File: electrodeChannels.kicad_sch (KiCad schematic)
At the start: 20 parts, among them Q17 PNP, Q2 NPN, Q20 PNP, Q5 PNP, Q8 PNP

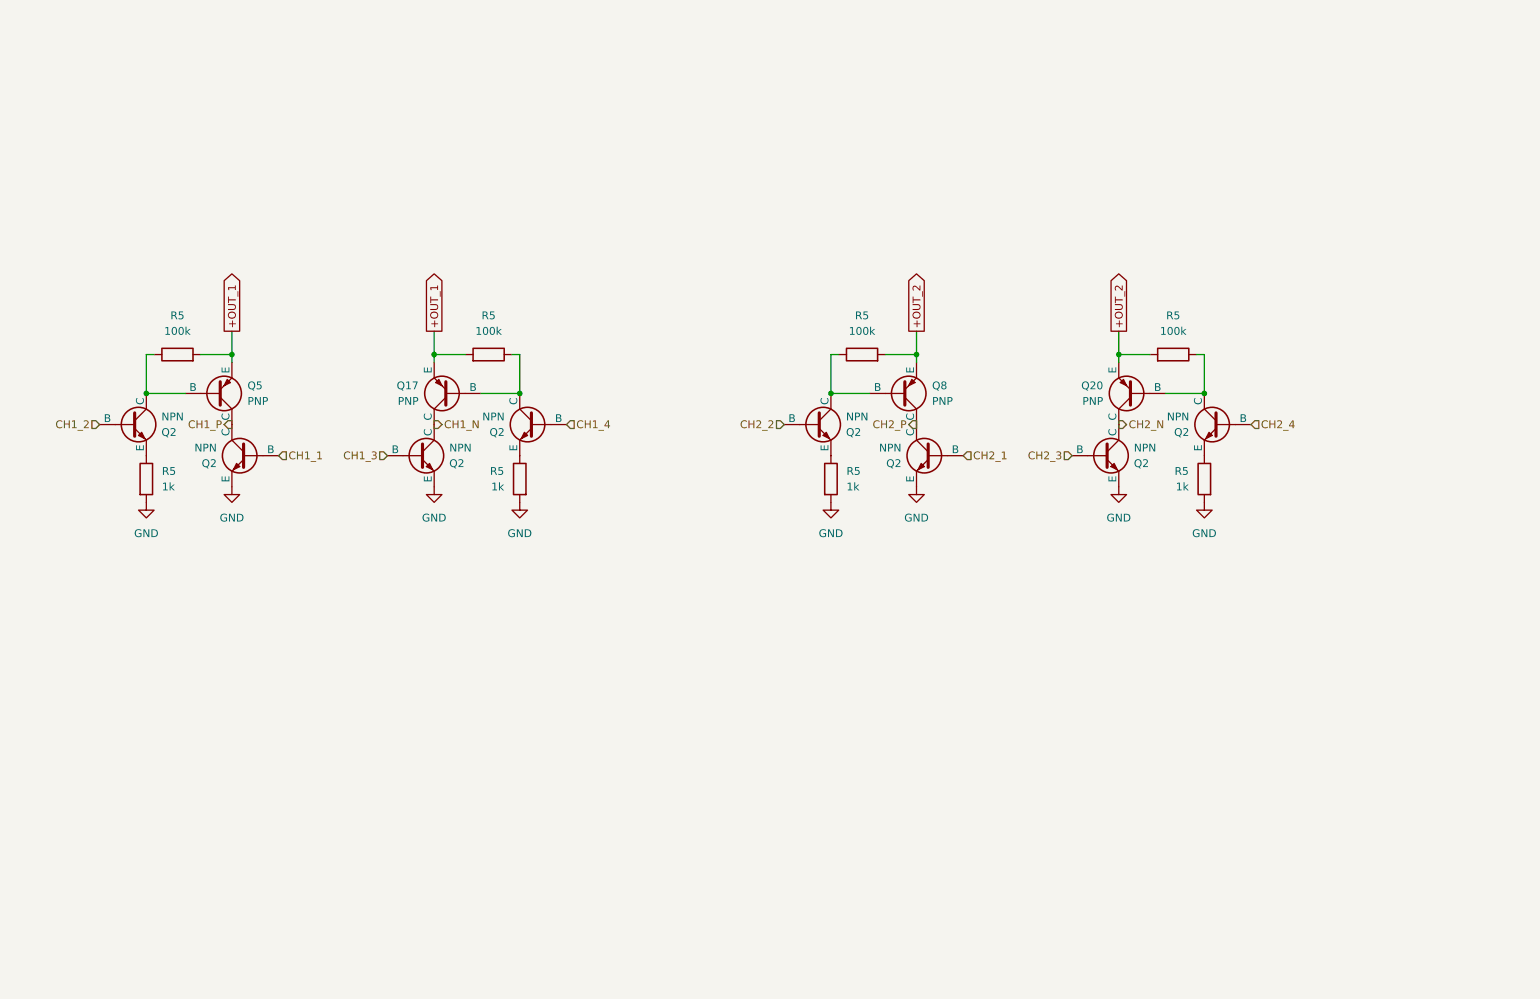
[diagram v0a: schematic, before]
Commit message: v3: removed digital potentiometer, added 8 discrete resistors and one GPIO expander
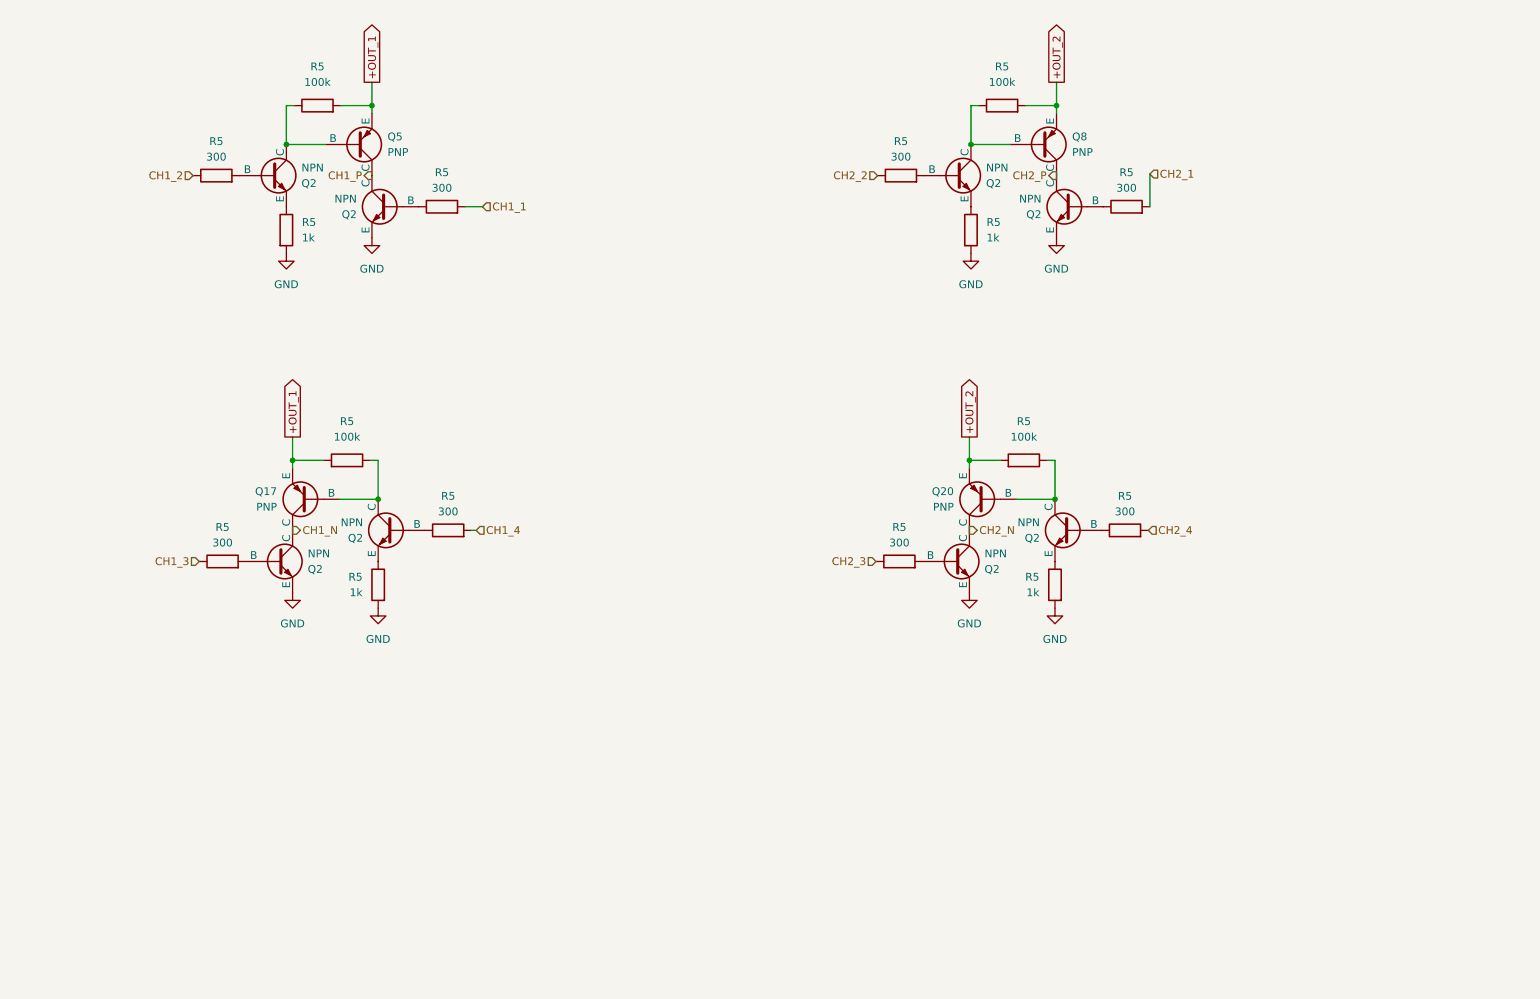
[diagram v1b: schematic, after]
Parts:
- added R5 (x8): 300, Resistor_SMD:R_0402_1005Metric, symbol Device:R
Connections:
- net CH1_1: now also R5.2; no longer Q2.1 (B)
- net CH1_2: now also R5.1; no longer Q2.1 (B)
- net CH1_3: now also R5.1; no longer Q2.1 (B)
- net CH1_4: now also R5.2; no longer Q2.1 (B)
- net CH2_1: now also R5.2; no longer Q2.1 (B)
- net CH2_2: now also R5.1; no longer Q2.1 (B)
- net CH2_3: now also R5.1; no longer Q2.1 (B)
- net CH2_4: now also R5.2; no longer Q2.1 (B)
- new net: Q2.1 (B), R5.1 (x4)
- new net: Q2.1 (B), R5.2 (x4)
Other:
- moved on the sheet: Q17, Q2, Q20, Q5, Q8, R5

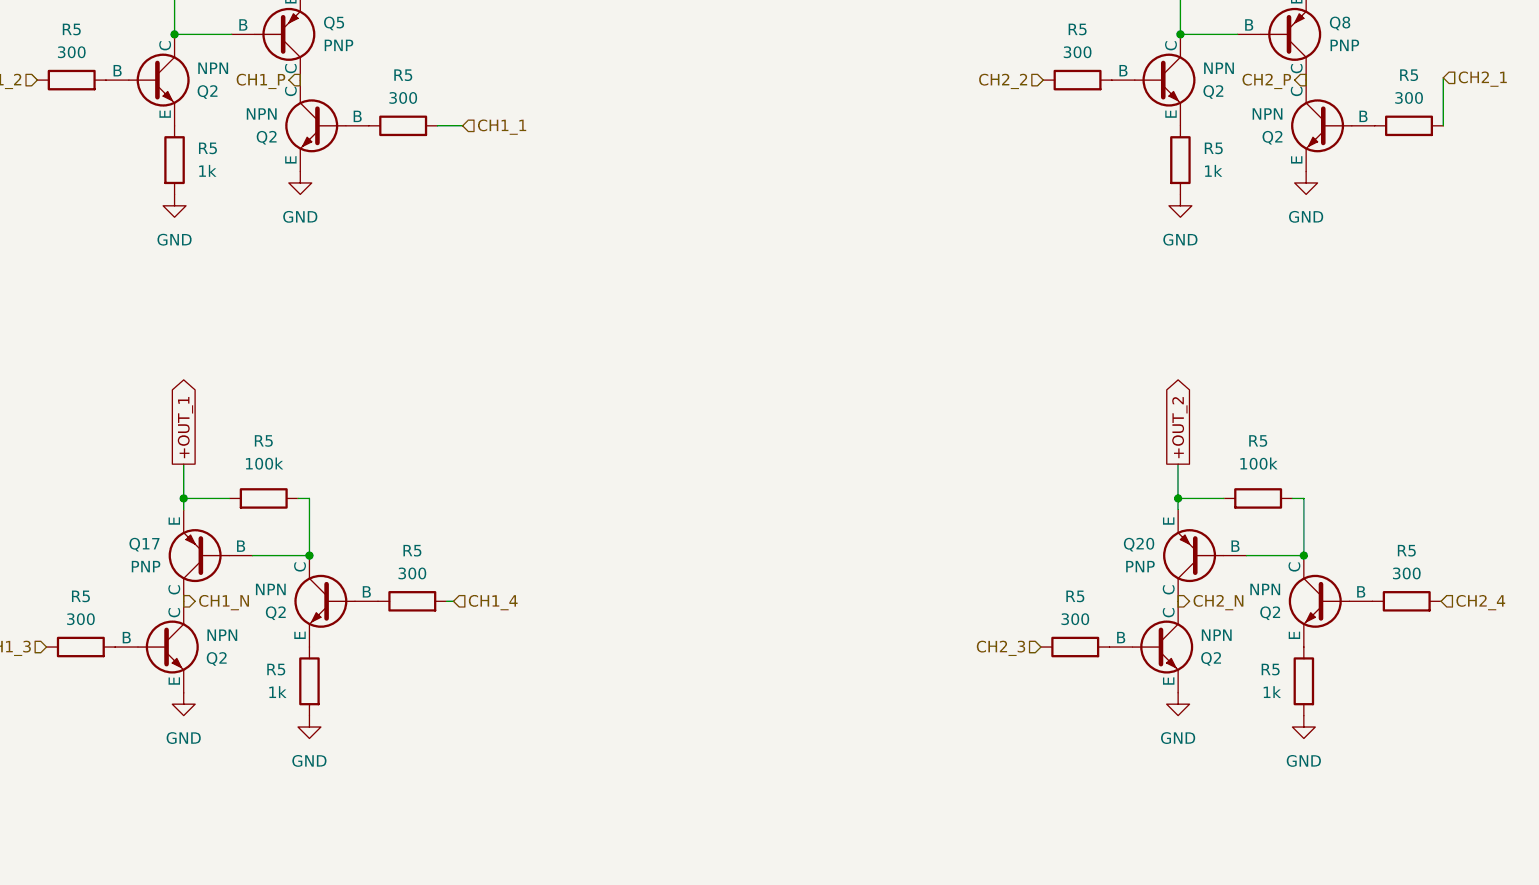
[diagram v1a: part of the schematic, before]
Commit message: version 4: changed GPIO expander, added current sense resistor to electrodes, added buzzer pins, fixed some gpio inputs that needs to be pulled high, added battery charge detection, added battery level measurement feature
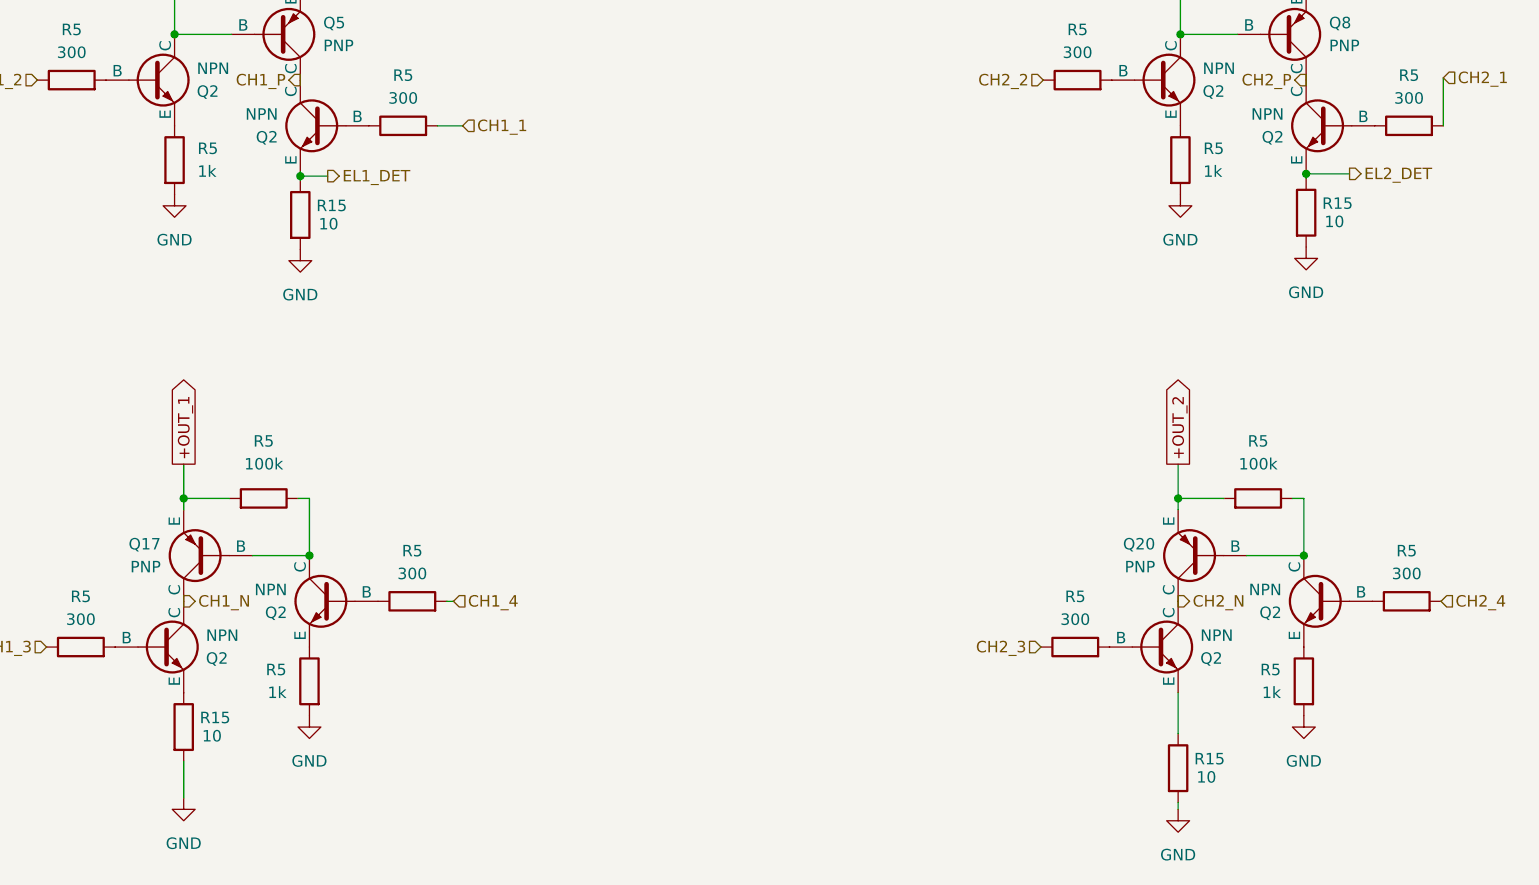
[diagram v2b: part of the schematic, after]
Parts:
- added R15 (x4): 10, Resistor_SMD:R_0402_1005Metric, symbol Device:R
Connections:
- net GND: now also R15.2, R15.2, R15.2, R15.2; no longer Q2.2 (E), Q2.2 (E), Q2.2 (E), Q2.2 (E)
- new net: Q2.2 (E), R15.1 (x2)
- new net EL1_DET: Q2.2 (E), R15.1
- new net EL2_DET: Q2.2 (E), R15.1

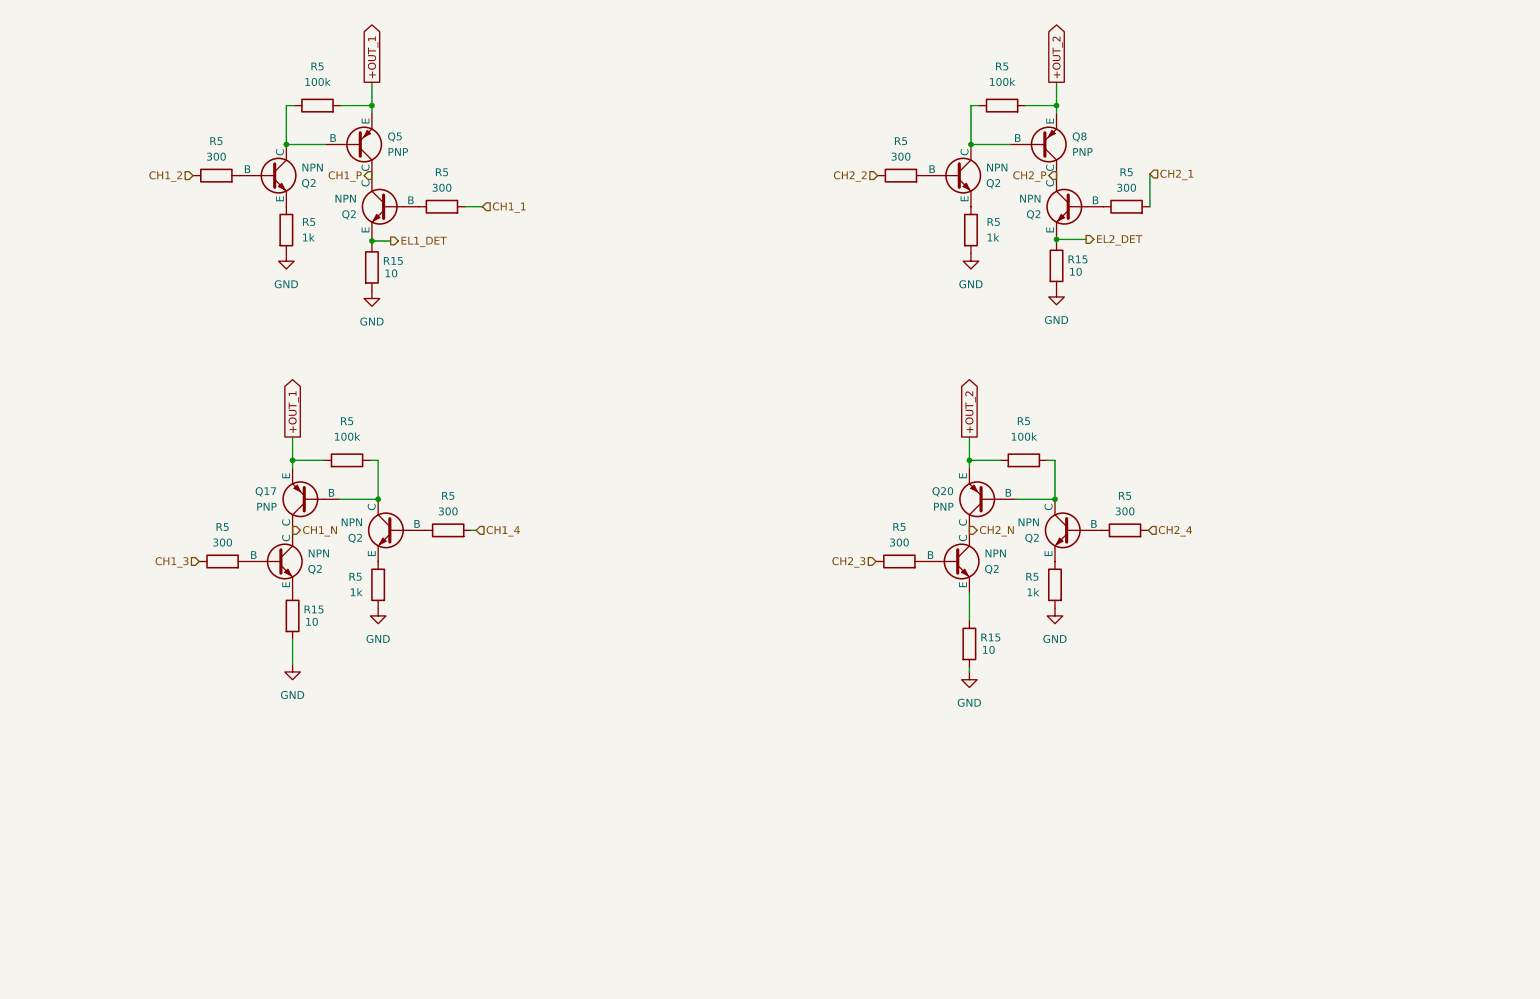
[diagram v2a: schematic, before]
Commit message: version 5: replaced ESP32-WROVER module with ESP-Mini, removed 2.5mm plugs, changed USB connector and routed electrode signals on it, added RC snubber circuit to boost converter and output caps to reduce switching loop
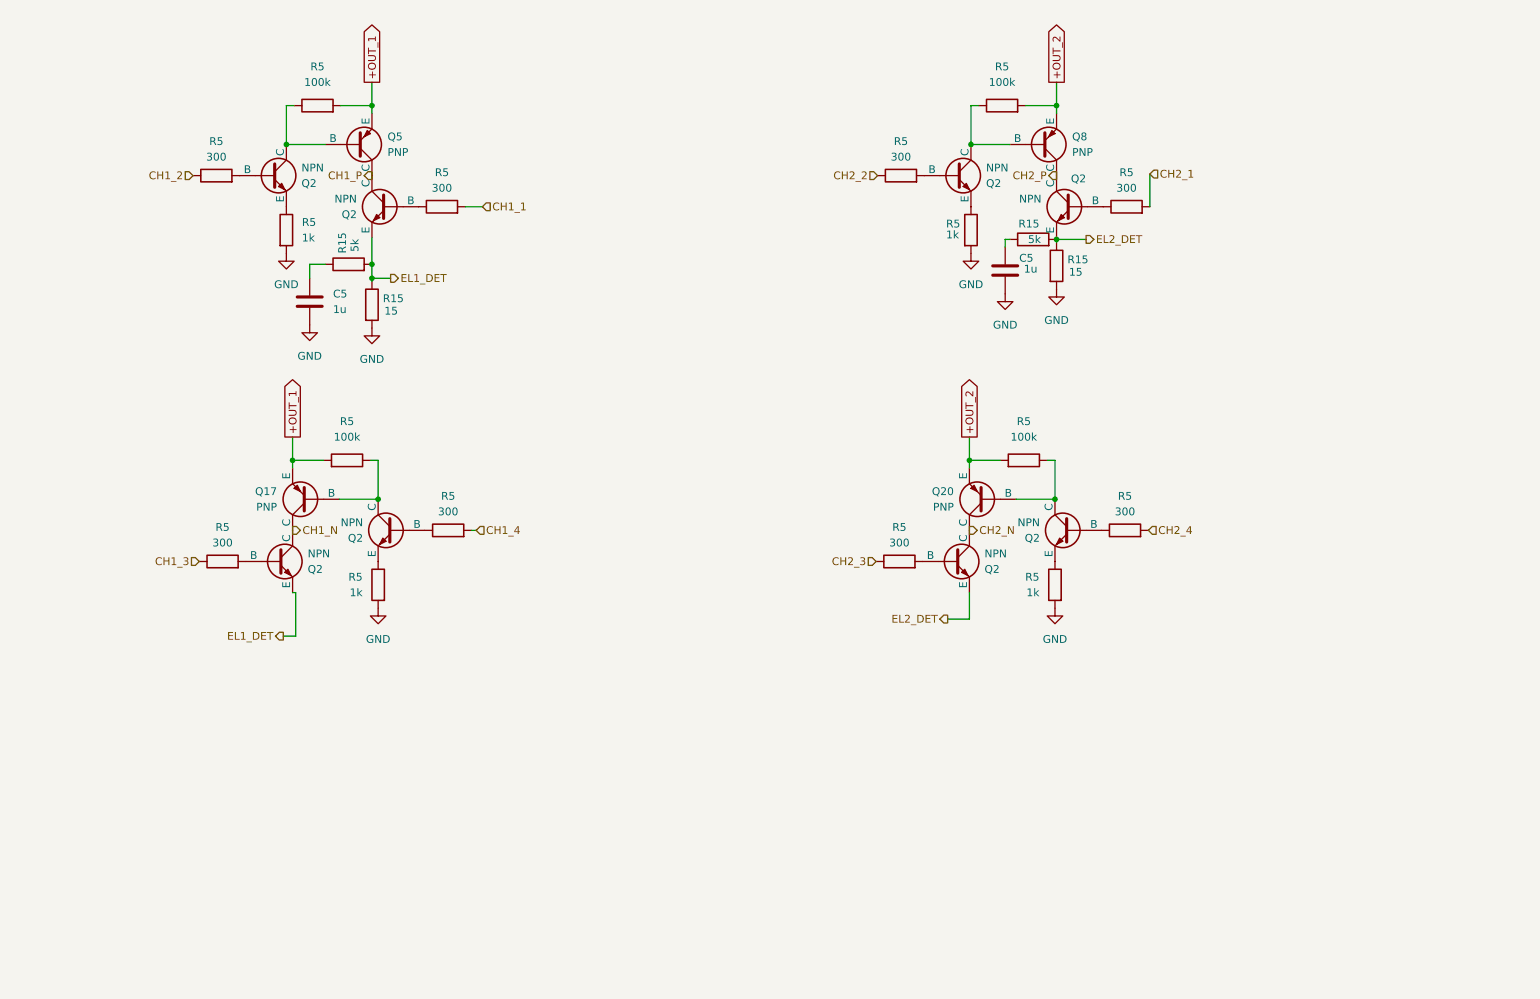
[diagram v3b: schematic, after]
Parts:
- removed R15 (x2): 10, Resistor_SMD:R_0402_1005Metric, symbol Device:R
- added C5 (x2): 1u, Capacitor_SMD:C_0603_1608Metric, symbol Device:C
- added R15 (x2): 5k, Resistor_SMD:R_0402_1005Metric, symbol Device:R
- Q2: Long Description Bipolar (BJT) Transistor NPN 60 V 2 A 100MHz 460 mW Surface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 -> Bipolar (BJT) Transistor NPN 60 V 1 A 150MHz 460 mW Surface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; Manufacturer On Semiconductor -> Diodes Incorporated; Manufacturer Part Number NSS60201LT1G -> DNBT8105-7
- R15: value 10 -> 15; Long Description 10 Ohms ±0.1% 0.063W, 1/16W Chip Resistor 0402 (1005 Metric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 -> 15 Ohms ±0.1% 0.063W, 1/16W Chip Resistor 0402 (1005 Metric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; Manufacturer Part Number RT0402BRD0710RL -> RT0402BRD0715RL
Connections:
- net EL1_DET: now also Q2.2 (E), R15.2
- net EL2_DET: now also Q2.2 (E), R15.2
- net GND: now also C5.2, C5.2
- new net: C5.1, R15.1 (x2)
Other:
- moved on the sheet: R15

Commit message: Fixed electrode detection mechanism, modified position of USB Type-C port
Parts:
- removed C5 (x2): 1u, Capacitor_SMD:C_0603_1608Metric, symbol Device:C
- removed R15 (x2): 15, Resistor_SMD:R_0402_1005Metric, symbol Device:R
- removed R15 (x2): 5k, Resistor_SMD:R_0402_1005Metric, symbol Device:R
- added Q2 (x4): NPN, Package_TO_SOT_SMD:SOT-23, symbol Simulation_SPICE:NPN
- added Q23, Q25, Q27, Q29: PNP, Package_TO_SOT_SMD:SOT-23, symbol Simulation_SPICE:PNP
- added R12 (x4): 1M, Resistor_SMD:R_0402_1005Metric, symbol Device:R
- added R49 (x2): 10k, Resistor_SMD:R_0402_1005Metric, symbol Device:R
- added R5 (x4): 300, Resistor_SMD:R_0402_1005Metric, symbol Device:R
- added R5 (x4): 100k, Resistor_SMD:R_0402_1005Metric, symbol Device:R
- added R5 (x4): 1k, Resistor_SMD:R_0402_1005Metric, symbol Device:R
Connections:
- net CH1_N: now also Q29.2 (E), R12.1, R5.2
- net CH1_P: now also Q27.3 (C), R12.1
- net CH2_N: now also Q23.2 (E), R12.1, R5.2
- net CH2_P: now also Q25.3 (C), R12.1
- net EL1_DET: now also Q29.3 (C), R49.1; no longer Q2.2 (E), Q2.2 (E)
- net EL2_DET: now also Q23.3 (C), R49.1; no longer Q2.2 (E), Q2.2 (E)
- net GND: now also Q2.2 (E), Q2.2 (E), Q2.2 (E), Q2.2 (E), R12.2, R12.2, R12.2, R12.2, R49.2, R49.2, R5.2, R5.2, R5.2, R5.2
- new net: Q2.1 (B), R5.2 (x4)
- new net: Q2.3 (C), Q27.1 (B), R5.1
- new net: Q2.2 (E), R5.1 (x4)
- new net: Q2.3 (C), Q29.1 (B), R5.1
- new net: Q2.3 (C), Q25.1 (B), R5.1
- new net: Q2.3 (C), Q23.1 (B), R5.1
- new net +3.3V: Q25.2 (E), Q27.2 (E), R5.2, R5.2
- new net CH1_EL_DET: R5.1, R5.1
- new net CH2_EL_DET: R5.1, R5.1
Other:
- moved on the sheet: Q2, Q20, Q8, R5
